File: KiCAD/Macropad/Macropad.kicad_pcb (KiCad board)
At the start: 2 copper layers, 100 x 100 mm, 33 parts, among them M1 MountingHole_3.5mm_Pad, M2 MountingHole_3.5mm_Pad, M3 MountingHole_3.5mm_Pad, M4 MountingHole_3.5mm_Pad, SW1 SW_Push_45deg, SW2 SW_Push_45deg, SW3 SW_Push_45deg, SW4 SW_Push_45deg, SW5 SW_Push_45deg, SW6 SW_Push_45deg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

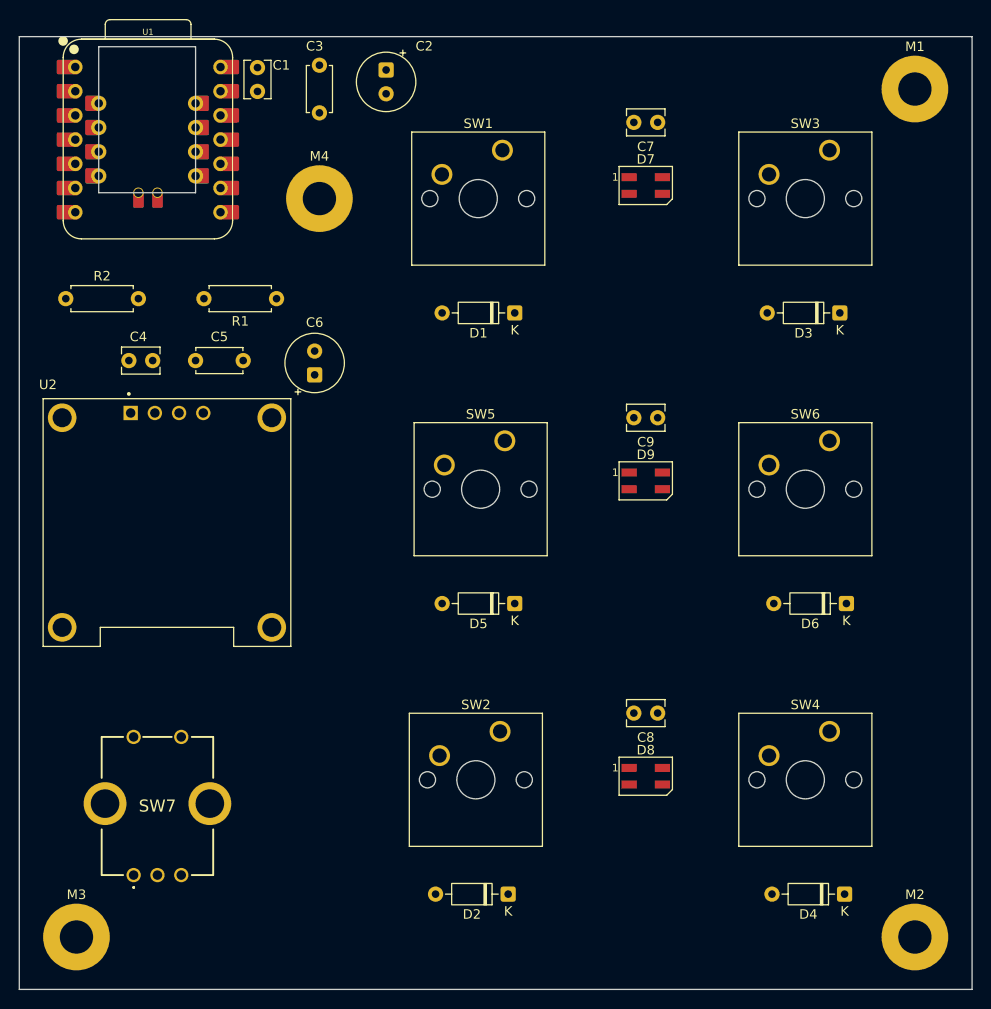
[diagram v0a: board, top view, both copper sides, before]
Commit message: Finished board wiring, layout, silkscreen, removed unneeded files, added case 3D model.
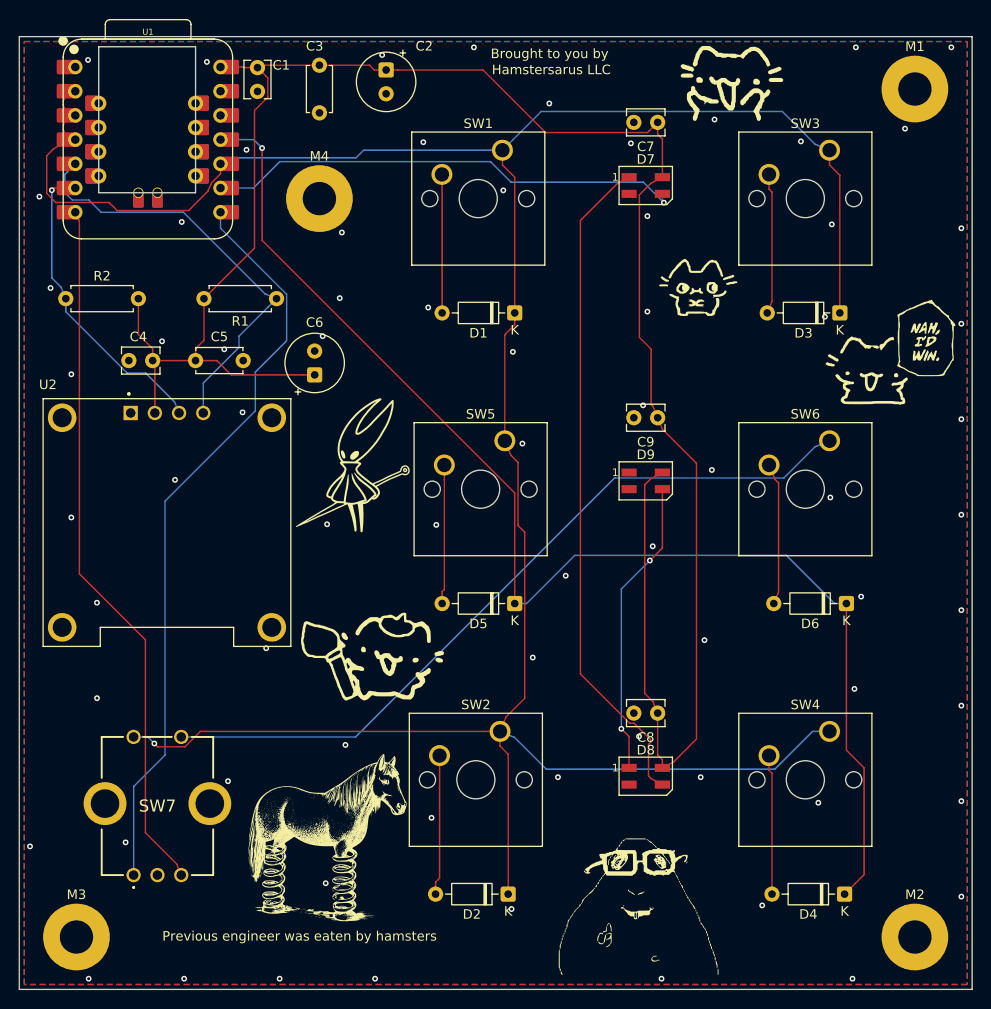
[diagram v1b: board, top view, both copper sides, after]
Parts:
- added Brought to you by Hamstersarus LLC: LOGO, LOGO, F.Cu at (135.0, 95.0)
- added G***: LOGO, LOGO, F.Cu at (191.0, 83.3)
- added G***: LOGO, LOGO, F.Cu at (138.0, 115.0)
- added G***: LOGO, LOGO, F.Cu at (171.0, 76.0)
- added G***: LOGO, LOGO, F.Cu at (174.5, 55.5)
- added G***: LOGO, LOGO, F.Cu at (164.0, 138.5)
- added G***: LOGO, LOGO, F.Cu at (132.5, 134.5)
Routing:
- net COL0: track 0.00 -> 277.8 mm, vias 0 -> 1
- net +5V: track 0.00 -> 219.1 mm
- net ROW1: track 0.00 -> 134.6 mm, vias 0 -> 1
- net ROTENCS2: track 0.00 -> 80.8 mm
- net Net-(SW7-CW): track 0.00 -> 79.1 mm
- net Net-(SW7-CCW): track 0.00 -> 74.5 mm
- net Net-(D7-DOUT): track 0.00 -> 70.4 mm
- net NEOIN: track 0.00 -> 50.5 mm, vias 0 -> 1
- net Net-(U1-P6_SDA_D4): track 0.00 -> 45.4 mm
- net Net-(U1-P7_SCL_D5): track 0.00 -> 31.6 mm, vias 0 -> 1
- net Net-(D8-DOUT): track 0.00 -> 31.4 mm, vias 0 -> 2
- net Net-(D6-A): track 0.00 -> 14.9 mm
- net Net-(D3-A): track 0.00 -> 14.8 mm
- net Net-(D2-A): track 0.00 -> 14.7 mm
- net Net-(D4-A): track 0.00 -> 14.7 mm
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- added copper zone on B.Cu, net GND
- added copper zone on F.Cu, net GND
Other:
- board text added: "Brought to you by"
- board text added: "Hamstersarus LLC"
- board text added: "Previous engineer was eaten by hamsters"

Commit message: Updated schematic and layout with new EC11 rotary encoder.
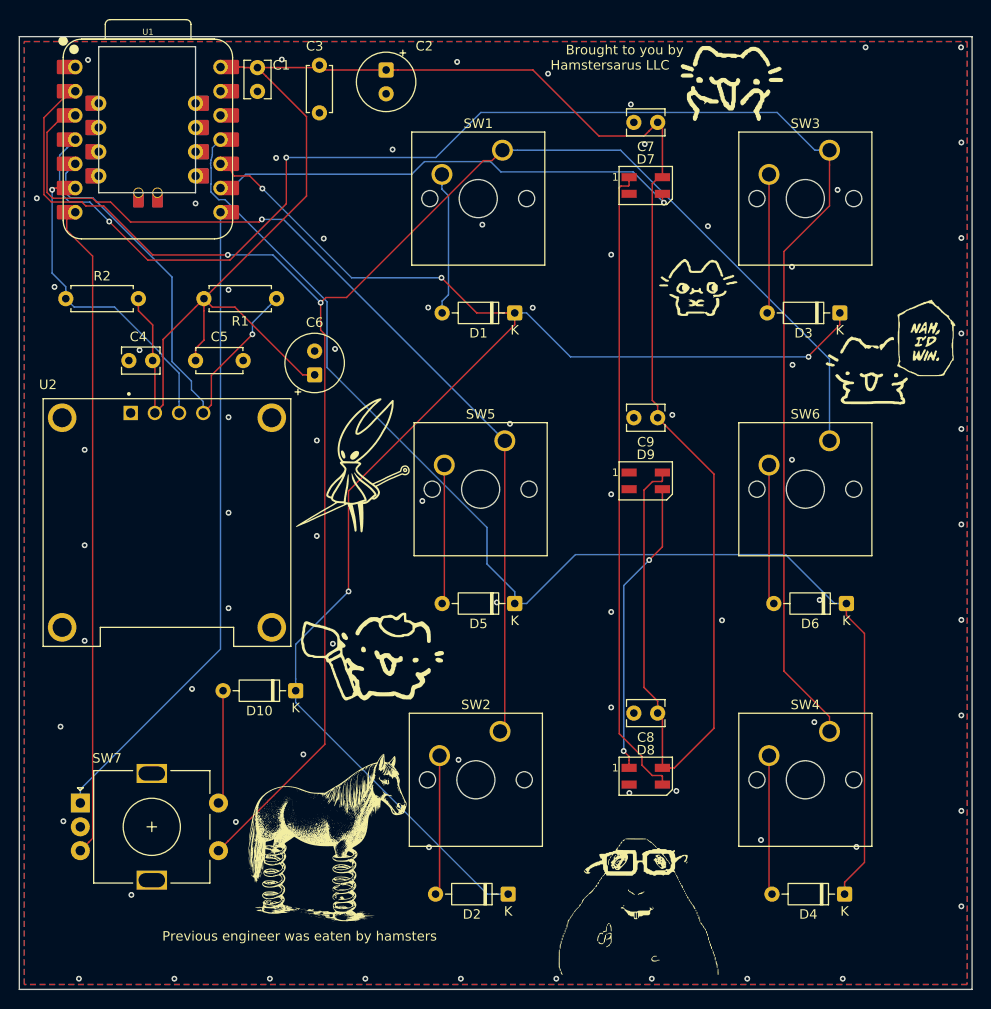
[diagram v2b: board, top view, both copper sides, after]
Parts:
- removed M1, M2, M3, M4: MountingHole_3.5mm_Pad, MountingHole:MountingHole_3.5mm_Pad
- added D10: 1N4148, Diode_THT:D_DO-35_SOD27_P7.62mm_Horizontal, F.Cu at (129.0, 118.6)
- SW7: value EC1110120201 -> RotaryEncoder_Switch; footprint EC1110120201_Rotary_Encoder:EC1110120201 -> Rotary_Encoder:RotaryEncoder_Alps_EC11E-Switch_Vertical_H20mm
- moved SW7 9.41 mm to (106.4, 130.4)
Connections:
- D1 pad 1: COL0 -> ROW0
- D2 pad 1: COL0 -> ROW0
- D3 pad 1: COL0 -> ROW0
- SW1 pad 1: COL0 -> COL2
- SW2 pad 1: COL0 -> COL1
- SW5 pad 1: COL0 -> COL1
- SW6 pad 1: ROTENCS2 -> COL2
- U1 pad 10: COL0 -> ROW0
- U1 pad 2: COL0 -> COL2
- U1 pad 3: COL0 -> COL1
- U1 pad 7: Net-(SW7-CCW) -> Net-(U1-P0_D6_TX)
- U1 pad 8: Net-(SW7-CW) -> Net-(U1-P1_D7_RX)
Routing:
- net COL2: track 0.00 -> 185.7 mm, vias 0 -> 2
- net ROW0: track 0.00 -> 156.6 mm, vias 0 -> 4
- net COL0: track 277.8 -> 165.8 mm, vias 1 -> 2
- net COL1: track 0.00 -> 99.0 mm, vias 0 -> 1
- net Net-(SW7-CW): track 79.1 -> 0.00 mm
- net Net-(SW7-CCW): track 74.5 -> 0.00 mm
- net ROTENCS2: track 80.8 -> 12.0 mm
- net Net-(U1-P0_D6_TX): track 0.00 -> 68.7 mm
- net Net-(U1-P1_D7_RX): track 0.00 -> 68.1 mm
- net +5V: track 219.1 -> 235.8 mm
- net Net-(U1-P6_SDA_D4): track 45.4 -> 49.1 mm, vias 0 -> 1
- net Net-(D7-DOUT): track 70.4 -> 67.1 mm
- net Net-(U1-P7_SCL_D5): track 31.6 -> 33.1 mm
- net ROW1: track 134.6 -> 133.9 mm, vias 1 -> 0
- net Net-(D1-A): track 14.5 -> 15.1 mm
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
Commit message: Update layout, schematic, and interactive BOM with part numbers
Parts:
- U1: value XIAO-RP2040-DIP -> XIAO-RP2350-DIP
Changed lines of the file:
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@@
 			(outputformat 1)
 			(mirror no)
-			(drillshape 1)
+			(drillshape 0)
 			(scaleselection 1)
-			(outputdirectory "")
+			(outputdirectory "Gerbers/")
 		)
 	)
@@
 			)
 		)
-		(property "Value" "XIAO-RP2040-DIP"
+		(property "Value" "XIAO-RP2350-DIP"
 			(at 0 0 90)
 			(unlocked yes)
@@
 			)
 		)
-		(property "Datasheet" "https://files.seeedstudio.com/wiki/XIAO-RP2040/res/rp2040_datasheet.pdf"
+		(property "Datasheet" "https://mm.digikey.com/Volume0/opasdata/d220001/medias/docus/8932/102010550.pdf"
 			(at 0 0 90)
 			(unlocked yes)
@@
 			)
 		)
-		(property "Description" ""
+		(property "Description" "High preformance microcontroller"
 			(at 0 0 90)
 			(unlocked yes)
@@
 			)
 		)
-		(property "Part_Number" "1597-102010428-ND"
+		(property "Part_Number" "1597-102010550-ND "
 			(at 0 0 90)
 			(unlocked yes)
@@
 					(thickness 0.15)
 				)
+			)
+		)
+		(property "Part_Number" "56-CCF554K70FKE36CT-ND"
+			(at 0 0 0)
+			(unlocked yes)
+			(layer "F.Fab")
+			(hide yes)
+			(effects
+				(font
+					(size 1 1)
+					(thickness 0.15)
+				)
+			)
+		)
+		(property "Vendor" "Digi-Key"
+			(at 0 0 0)
+			(unlocked yes)
+			(layer "F.Fab")
+			(hide yes)
+			(effects
+				(font
+					(size 1 1)
+					(thickness 0.15)
+				)

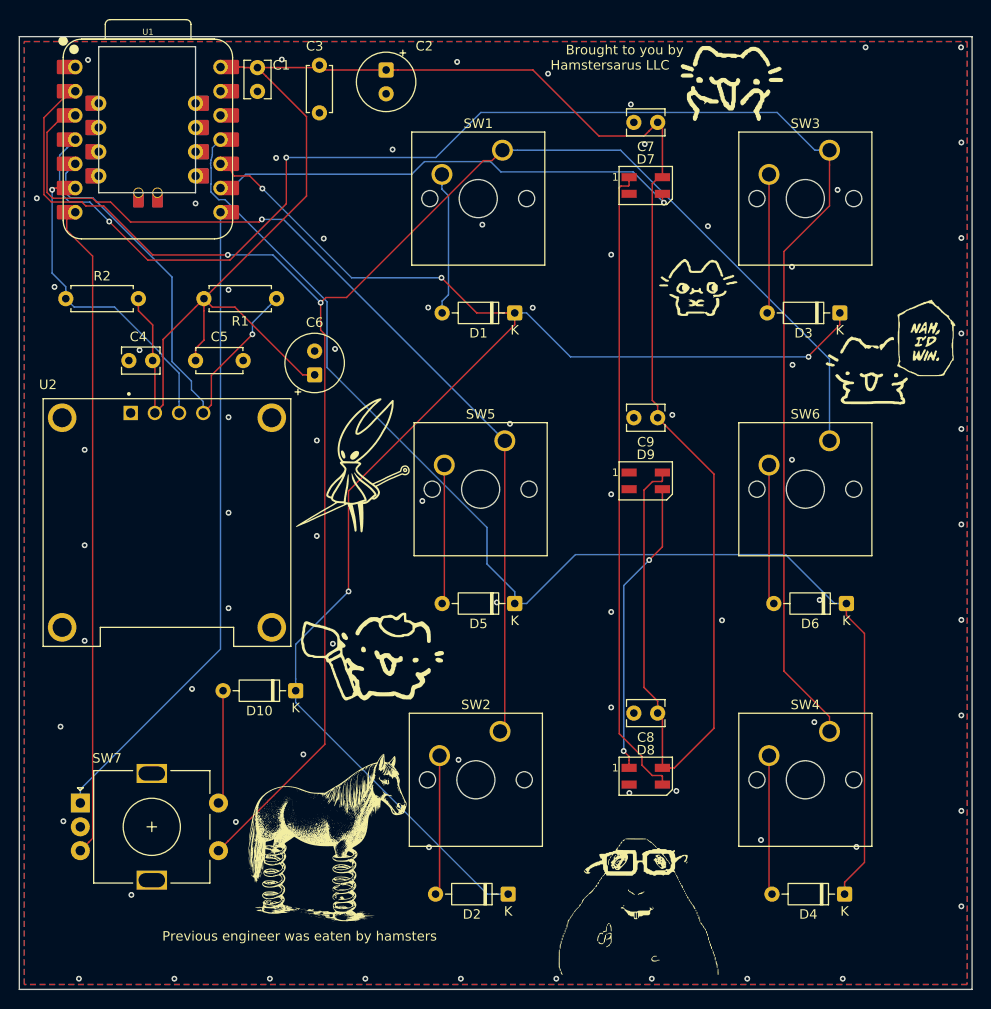
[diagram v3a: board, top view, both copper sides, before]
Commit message: Fixed a crossed wire issue and an issue with my microcontroller.
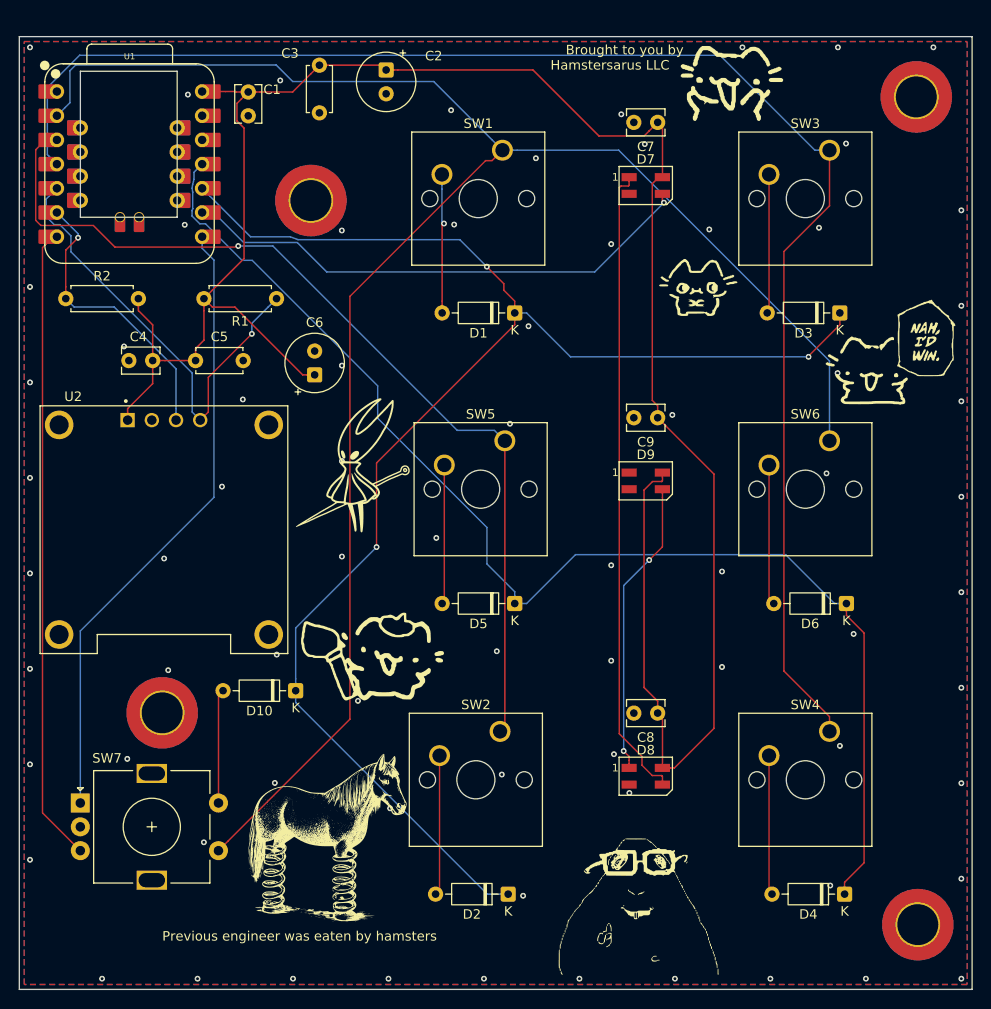
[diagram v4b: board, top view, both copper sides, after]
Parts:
- added REF1: MountingHole_4.3mm_M4_DIN965_Pad_TopBottom, MountingHole:MountingHole_4.3mm_M4_DIN965_Pad_TopBottom, F.Cu at (115.0, 121.0)
- added REF2: MountingHole_4.3mm_M4_DIN965_Pad_TopBottom, MountingHole:MountingHole_4.3mm_M4_DIN965_Pad_TopBottom, F.Cu at (194.3, 143.2)
- added REF3: MountingHole_4.3mm_M4_DIN965_Pad_TopBottom, MountingHole:MountingHole_4.3mm_M4_DIN965_Pad_TopBottom, F.Cu at (194.1, 56.3)
- added REF4: MountingHole_4.3mm_M4_DIN965_Pad_TopBottom, MountingHole:MountingHole_4.3mm_M4_DIN965_Pad_TopBottom, F.Cu at (130.6, 67.2)
- moved U1 3.21 mm to (111.6, 63.4)
- moved C1 2.74 mm to (124.0, 55.8)
- moved U2 0.81 mm to (115.2, 101.7)
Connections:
- U2 pad 1: GND -> +5V
- U2 pad 2: +5V -> GND
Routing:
- net +5V: track 235.8 -> 224.3 mm
- net COL2: track 185.7 -> 192.8 mm, vias 2 -> 0
- net COL0: track 165.8 -> 161.0 mm, vias 2 -> 0
- net NEOIN: track 50.5 -> 55.1 mm
- net Net-(U1-P7_SCL_D5): track 33.1 -> 30.5 mm
- net ROW0: track 156.6 -> 159.0 mm, vias 4 -> 3
- net Net-(U1-P0_D6_TX): track 68.7 -> 66.3 mm
- net Net-(U1-P1_D7_RX): track 68.1 -> 65.8 mm
- net Net-(U1-P6_SDA_D4): track 49.1 -> 47.9 mm
- net ROW1: track 133.9 -> 132.7 mm
- net Net-(D1-A): track 15.1 -> 14.7 mm, vias 0 -> 1
- net GND: vias 76 -> 74
